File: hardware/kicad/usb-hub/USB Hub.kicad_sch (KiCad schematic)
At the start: 82 parts, among them J1 USB_A, J10 Connector, USB-TYPE-C-16P, J2 Connector, USB-TYPE-C-16P, J3 USB_A, J4 USB_A, J5 Connector, USB-TYPE-C- vert, J6 USB_A, J7 From 12V supply, J8 B5B-XH-A_LF__SN_, J9 B5B-XH-A_LF__SN_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

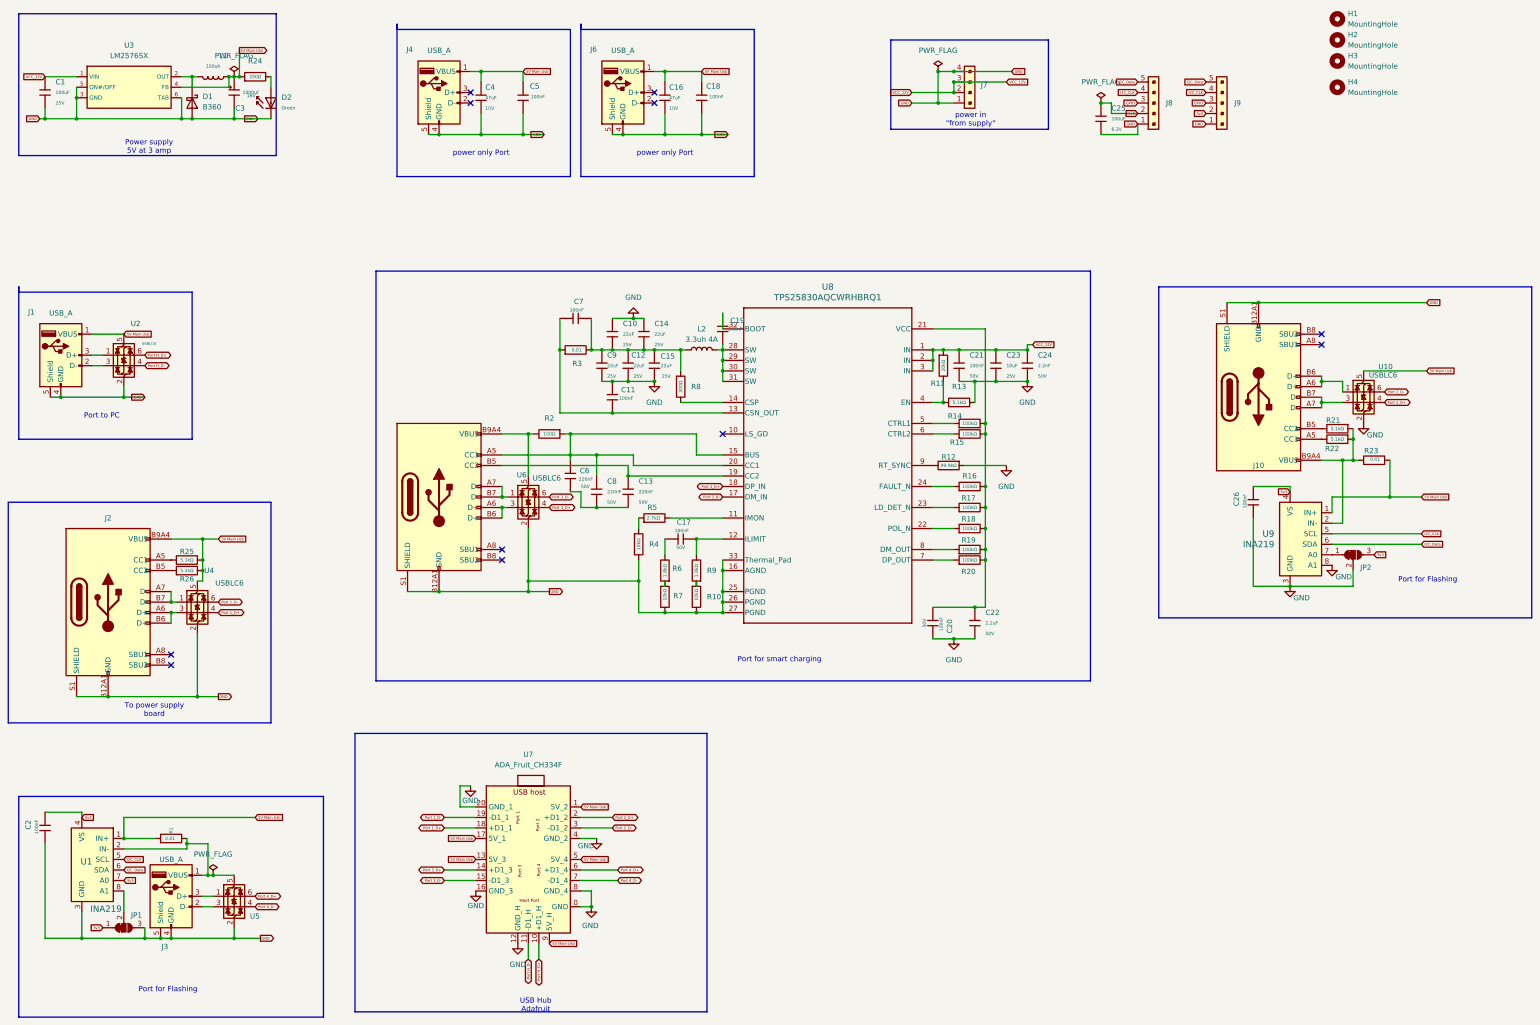
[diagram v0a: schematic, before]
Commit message: Revert "Add files via upload"
This reverts commit 9727bb8fcf1ad0520ca163fc3fe7730c7a9ac76a.
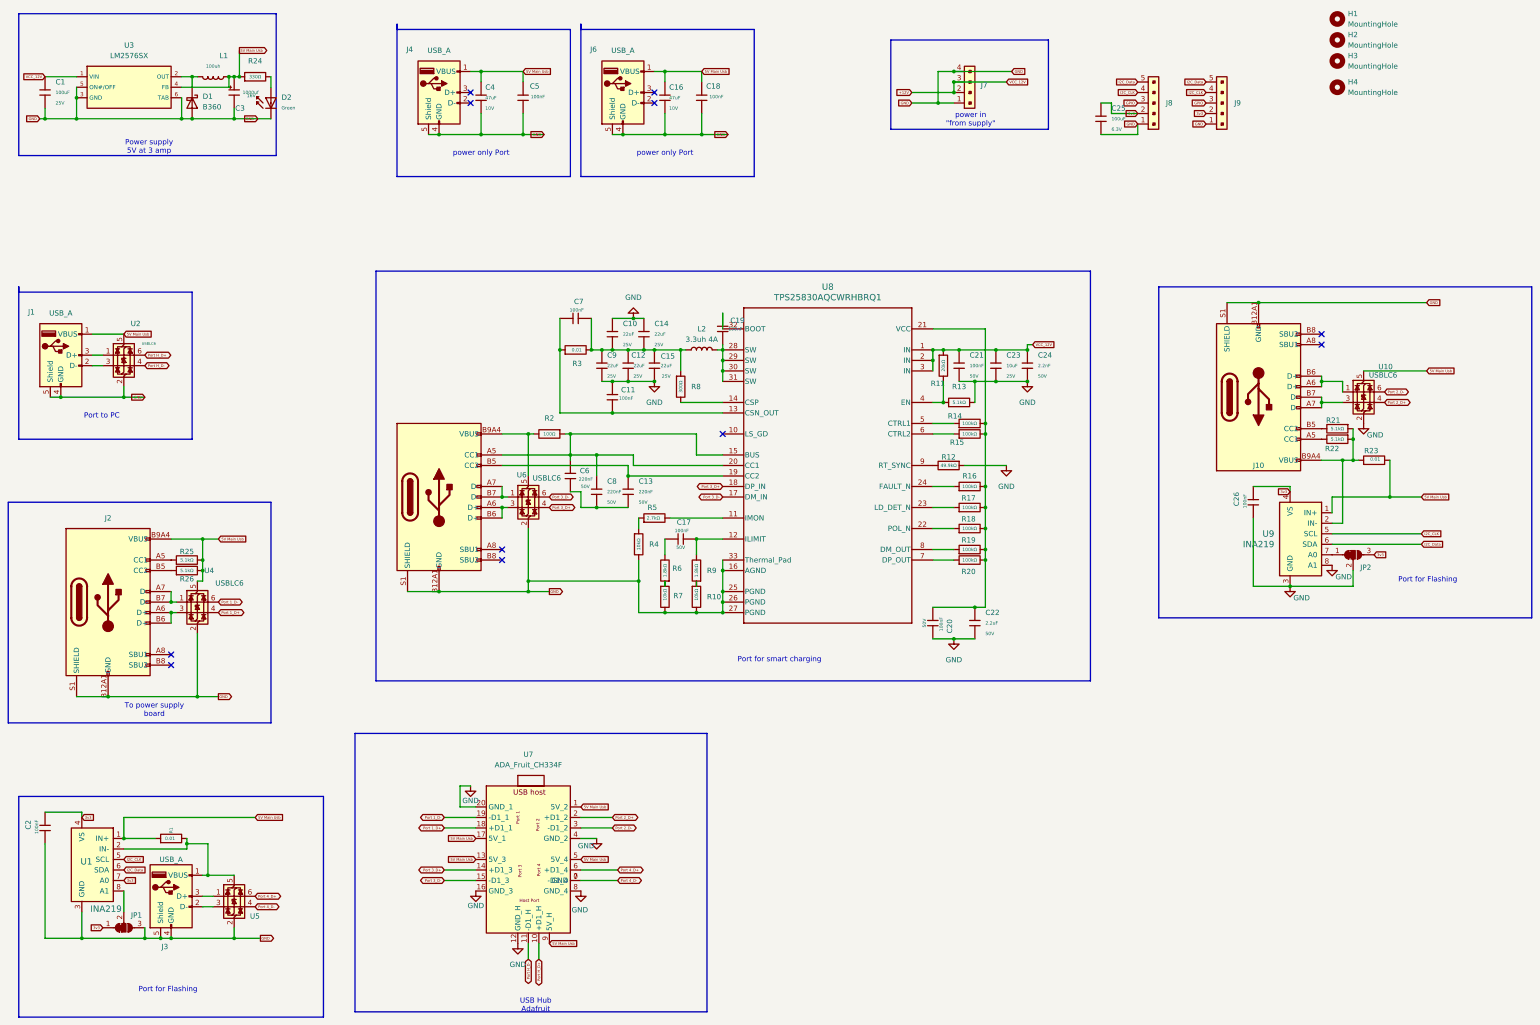
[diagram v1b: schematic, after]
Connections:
- net GND: no longer U7.0 (GND)
- net Port 4_D-: now also U7.0 (GND)
- net VCC_12V renamed +12V
